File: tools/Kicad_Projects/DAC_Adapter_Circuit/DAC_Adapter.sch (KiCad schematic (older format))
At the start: 13 parts, among them P1 CONN_01X05, P2 CONN_01X03, P3 CONN_01X02, P4 CONN_01X02, P5 CONN_01X02, U1 LM324N

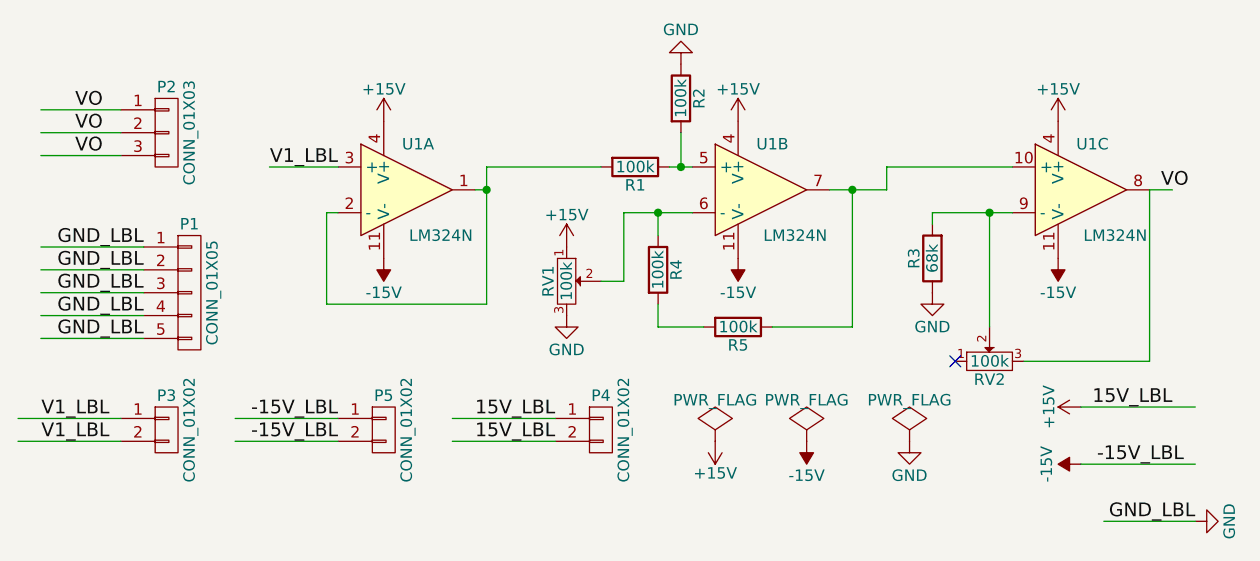
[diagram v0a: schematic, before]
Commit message: Added clone button functionality
* Also, DAC Adapter Circuit modifications are comitted #34
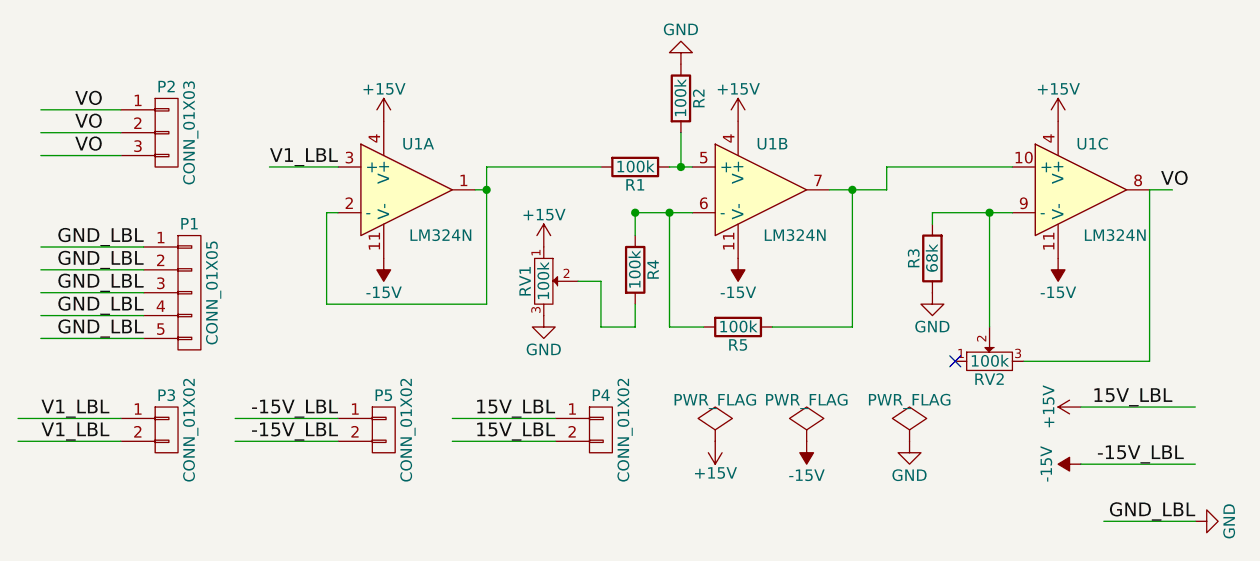
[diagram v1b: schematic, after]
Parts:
- RV1, RV2: footprint Potentiometers:Potentiometer_Bourns_3296Z_3-8Zoll_Angular_ScrewFront -> Potentiometers:Potentiometer_Bourns_3339H_Angular_ScrewUp
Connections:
- wire segments 43 -> 45
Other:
- moved on the sheet: R4, RV1
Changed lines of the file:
@@
 LIBS:contrib
 LIBS:valves
+LIBS:DAC_Adapter-cache
 EELAYER 25 0
 EELAYER END
@@
 L R R4
 U 1 1 5800248B
-P 5200 2350
-F 0 "R4" V 5280 2350 50  0000 C CNN
-F 1 "100k" V 5200 2350 50  0000 C CNN
-F 2 "Resistors_ThroughHole:Resistor_Horizontal_RM10mm" V 5130 2350 50  0001 C CNN
-F 3 "" H 5200 2350 50  0000 C CNN
-	1    5200 2350
+P 5100 2350
+F 0 "R4" V 5180 2350 50  0000 C CNN
+F 1 "100k" V 5100 2350 50  0000 C CNN
+F 2 "Resistors_ThroughHole:Resistor_Horizontal_RM10mm" V 5030 2350 50  0001 C CNN
+F 3 "" H 5100 2350 50  0000 C CNN
+	1    5100 2350
 	1    0    0    -1
 $EndComp
@@
 L POT RV1
 U 1 1 580B853A
-P 4800 2400
-F 0 "RV1" H 4800 2320 50  0000 C CNN
-F 1 "100k" H 4800 2400 50  0000 C CNN
-F 2 "Potentiometers:Potentiometer_Bourns_3296Z_3-8Zoll_Angular_ScrewFront" H 4800 2400 50  0001 C CNN
-F 3 "" H 4800 2400 50  0000 C CNN
-	1    4800 2400
+P 4700 2400
+F 0 "RV1" H 4700 2320 50  0000 C CNN
+F 1 "100k" H 4700 2400 50  0000 C CNN
+F 2 "Potentiometers:Potentiometer_Bourns_3339H_Angular_ScrewUp" H 4700 2400 50  0001 C CNN
+F 3 "" H 4700 2400 50  0000 C CNN
+	1    4700 2400
 	0    1    1    0
 $EndComp
@@
 L +15V #PWR09
 U 1 1 58C375C4
-P 4800 2250
-F 0 "#PWR09" H 4800 2100 50  0001 C CNN
-F 1 "+15V" H 4800 2390 50  0000 C CNN
-F 2 "" H 4800 2250 50  0000 C CNN
-F 3 "" H 4800 2250 50  0000 C CNN
-	1    4800 2250
+P 4700 2250
+F 0 "#PWR09" H 4700 2100 50  0001 C CNN
+F 1 "+15V" H 4700 2390 50  0000 C CNN
+F 2 "" H 4700 2250 50  0000 C CNN
+F 3 "" H 4700 2250 50  0000 C CNN
+	1    4700 2250
 	1    0    0    -1
 $EndComp
@@
 L GND #PWR010
 U 1 1 58C37706
-P 4800 2550
-F 0 "#PWR010" H 4800 2300 50  0001 C CNN
-F 1 "GND" H 4800 2400 50  0000 C CNN
-F 2 "" H 4800 2550 50  0000 C CNN
-F 3 "" H 4800 2550 50  0000 C CNN
-	1    4800 2550
+P 4700 2550
+F 0 "#PWR010" H 4700 2300 50  0001 C CNN
+F 1 "GND" H 4700 2400 50  0000 C CNN
+F 2 "" H 4700 2550 50  0000 C CNN
+F 3 "" H 4700 2550 50  0000 C CNN
+	1    4700 2550
 	1    0    0    -1
 $EndComp
@@
 F 0 "RV2" H 6650 2670 50  0000 C CNN
 F 1 "100k" H 6650 2750 50  0000 C CNN
-F 2 "Potentiometers:Potentiometer_Bourns_3296Z_3-8Zoll_Angular_ScrewFront" H 6650 2750 50  0001 C CNN
+F 2 "Potentiometers:Potentiometer_Bourns_3339H_Angular_ScrewUp" H 6650 2750 50  0001 C CNN
 F 3 "" H 6650 2750 50  0000 C CNN
 	1    6650 2750
@@
 	5300 1900 5300 1750
 Wire Wire Line
-	5050 2100 5350 2100
-Wire Wire Line
 	5700 2600 6050 2600
 Wire Wire Line
@@
 	5950 2000 6200 2000
 Wire Wire Line
-	5200 2600 5400 2600
-Wire Wire Line
-	5200 2100 5200 2200
-Wire Wire Line
-	5200 2600 5200 2500
-Wire Wire Line
-	5050 2100 5050 2400
-Wire Wire Line
-	5050 2400 4950 2400
-Connection ~ 5200 2100
+	5100 2600 5100 2500
+Wire Wire Line
+	4950 2400 4850 2400
 Wire Wire Line
 	6200 2000 6200 1900
@@
 	6650 2100 6650 2600
 Wire Wire Line
-	7350 2750 7350 2000
-Wire Wire Line
-	6800 2750 7350 2750
+	7350 2000 7350 2750
+Wire Wire Line
+	7350 2750 6800 2750
+Wire Wire Line
+	5100 2200 5100 2100
+Connection ~ 5100 2100
+Wire Wire Line
+	5400 2600 5250 2600
+Wire Wire Line
+	5250 2600 5250 2100
+Wire Wire Line
+	5100 2100 5350 2100
+Connection ~ 5250 2100
+Wire Wire Line
+	5100 2600 4950 2600
+Wire Wire Line
+	4950 2600 4950 2400
 $EndSCHEMATC
